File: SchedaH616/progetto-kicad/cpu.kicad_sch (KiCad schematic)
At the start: 81 parts, among them J301 UART0 debug, SW301 RESET, SW302 FEL, U301 H616, U302 TPD4E05U06DQA, U303 TPD4E05U06DQA, U304 TPD4E05U06DQA, U305 TPD4E05U06DQA, U306 TPD4E05U06DQA, U307 TPD4E05U06DQA, U308 TCA6416APWR, Y301 24MHz

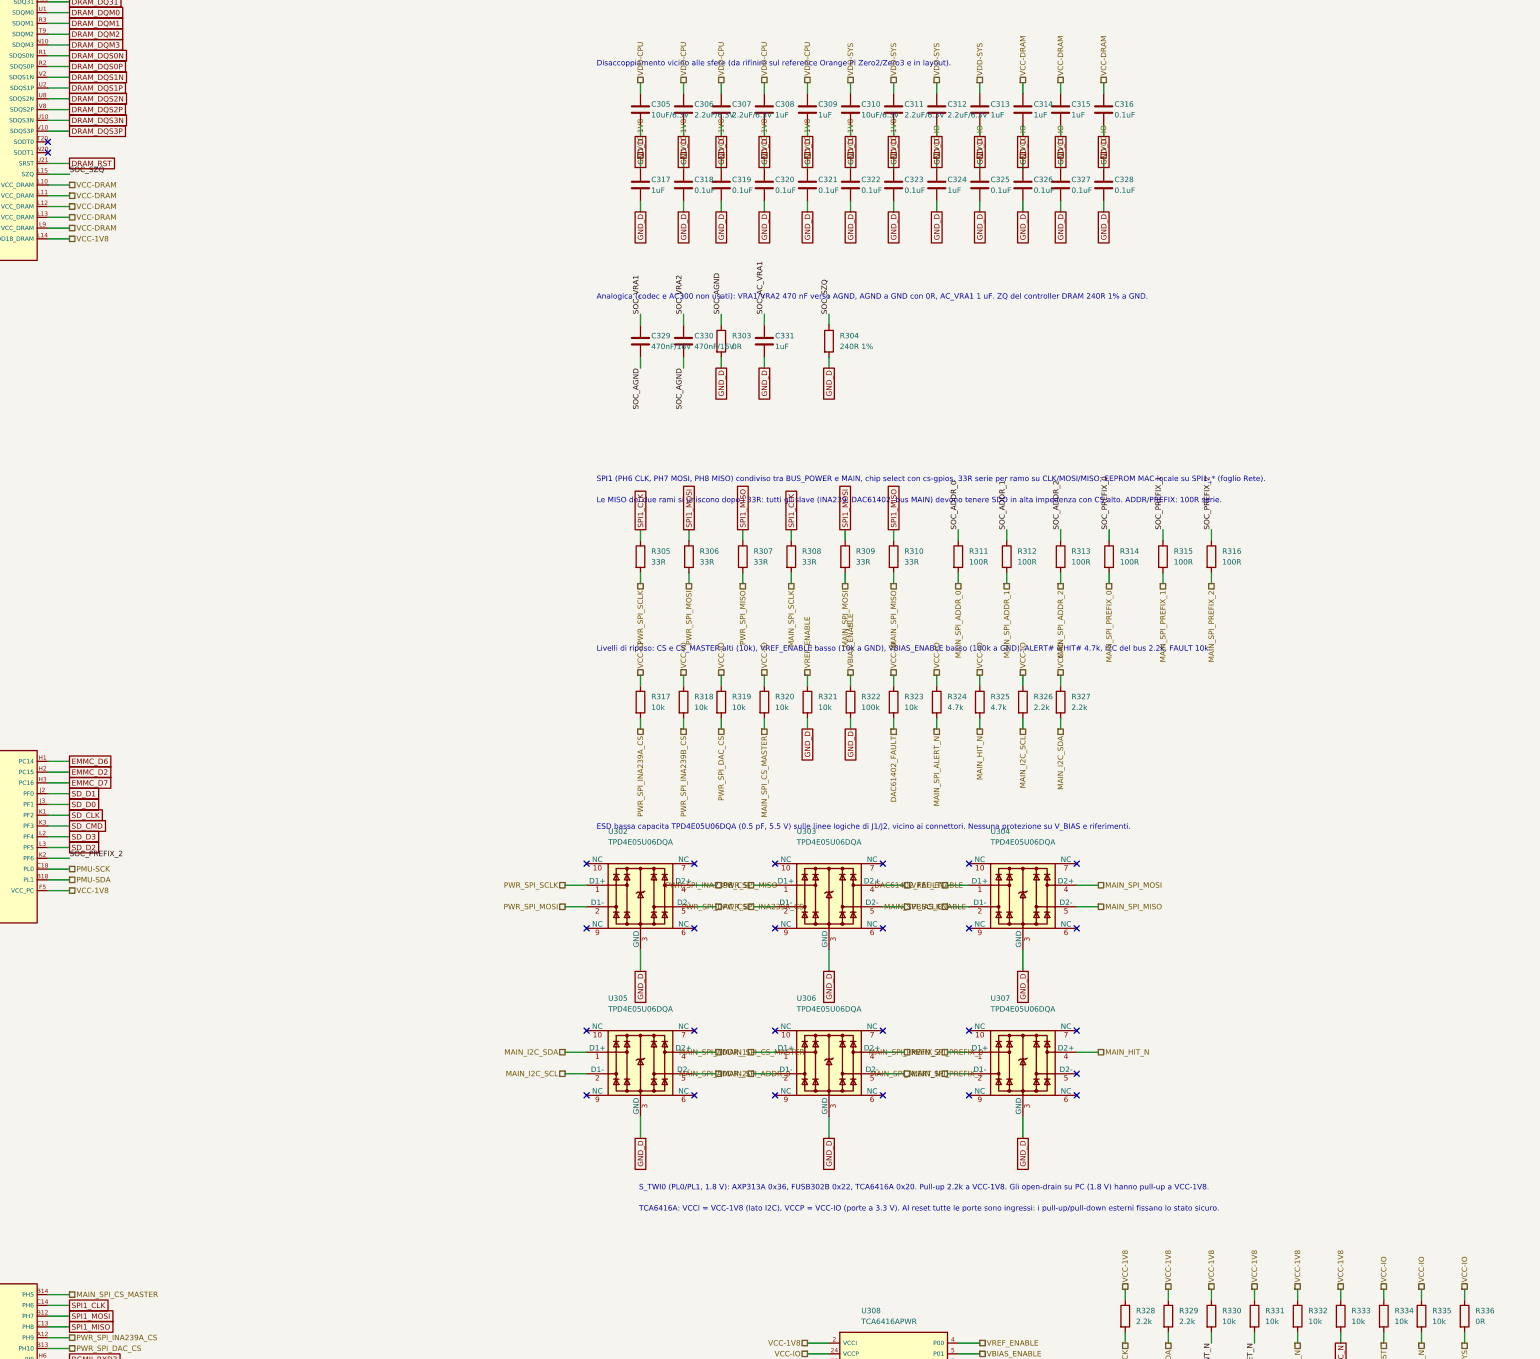
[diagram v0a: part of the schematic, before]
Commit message: SchedaH616: placement PCB 50x70 a 6 strati e modifiche allo schema
PCB (solo placement, niente piste), generato da generatori/build_pcb.sh:
- 50 x 70 mm, smussi 3 mm, 4 fori NPTH 2.2 mm con keepout, 6 strati
- H616 al centro, LPDDR4 sul lato DRAM, AXP313A vicino alla CPU, eMMC vicino ai pin PC
- connettori sui bordi, U.FL Wi-Fi e SMA GNSS su lati opposti
- disaccoppiamento di H616 e LPDDR4 sul bottom sotto le sfere
- regole: piste 5 mil, via-in-pad 0.25/0.15 sotto l'H616
- DRC: 0 violazioni (solo collegamenti da fare), parità schema/PCB ok

Schema (modifiche approvate):
- LPDDR4 confermata come scelta definitiva
- USB host di nuovo su USB-C solo host (Rp 22k, USBLC6-2, TPS2553)
- jack 5 V diretto su IN1 del TPS2121, tolto l'SS54, TPS56637 in Eco-mode
- LDO AP2112K-1.8 (C176944) dedicato a VCCQ eMMC e VCC_PC
- ERC 0

Libreria H616.pretty: serigrafia sui pad tolta, pioli di centraggio NPTH.

Co-Authored-By: Claude Opus 5.5 (1M context) <noreply@anthropic.com>
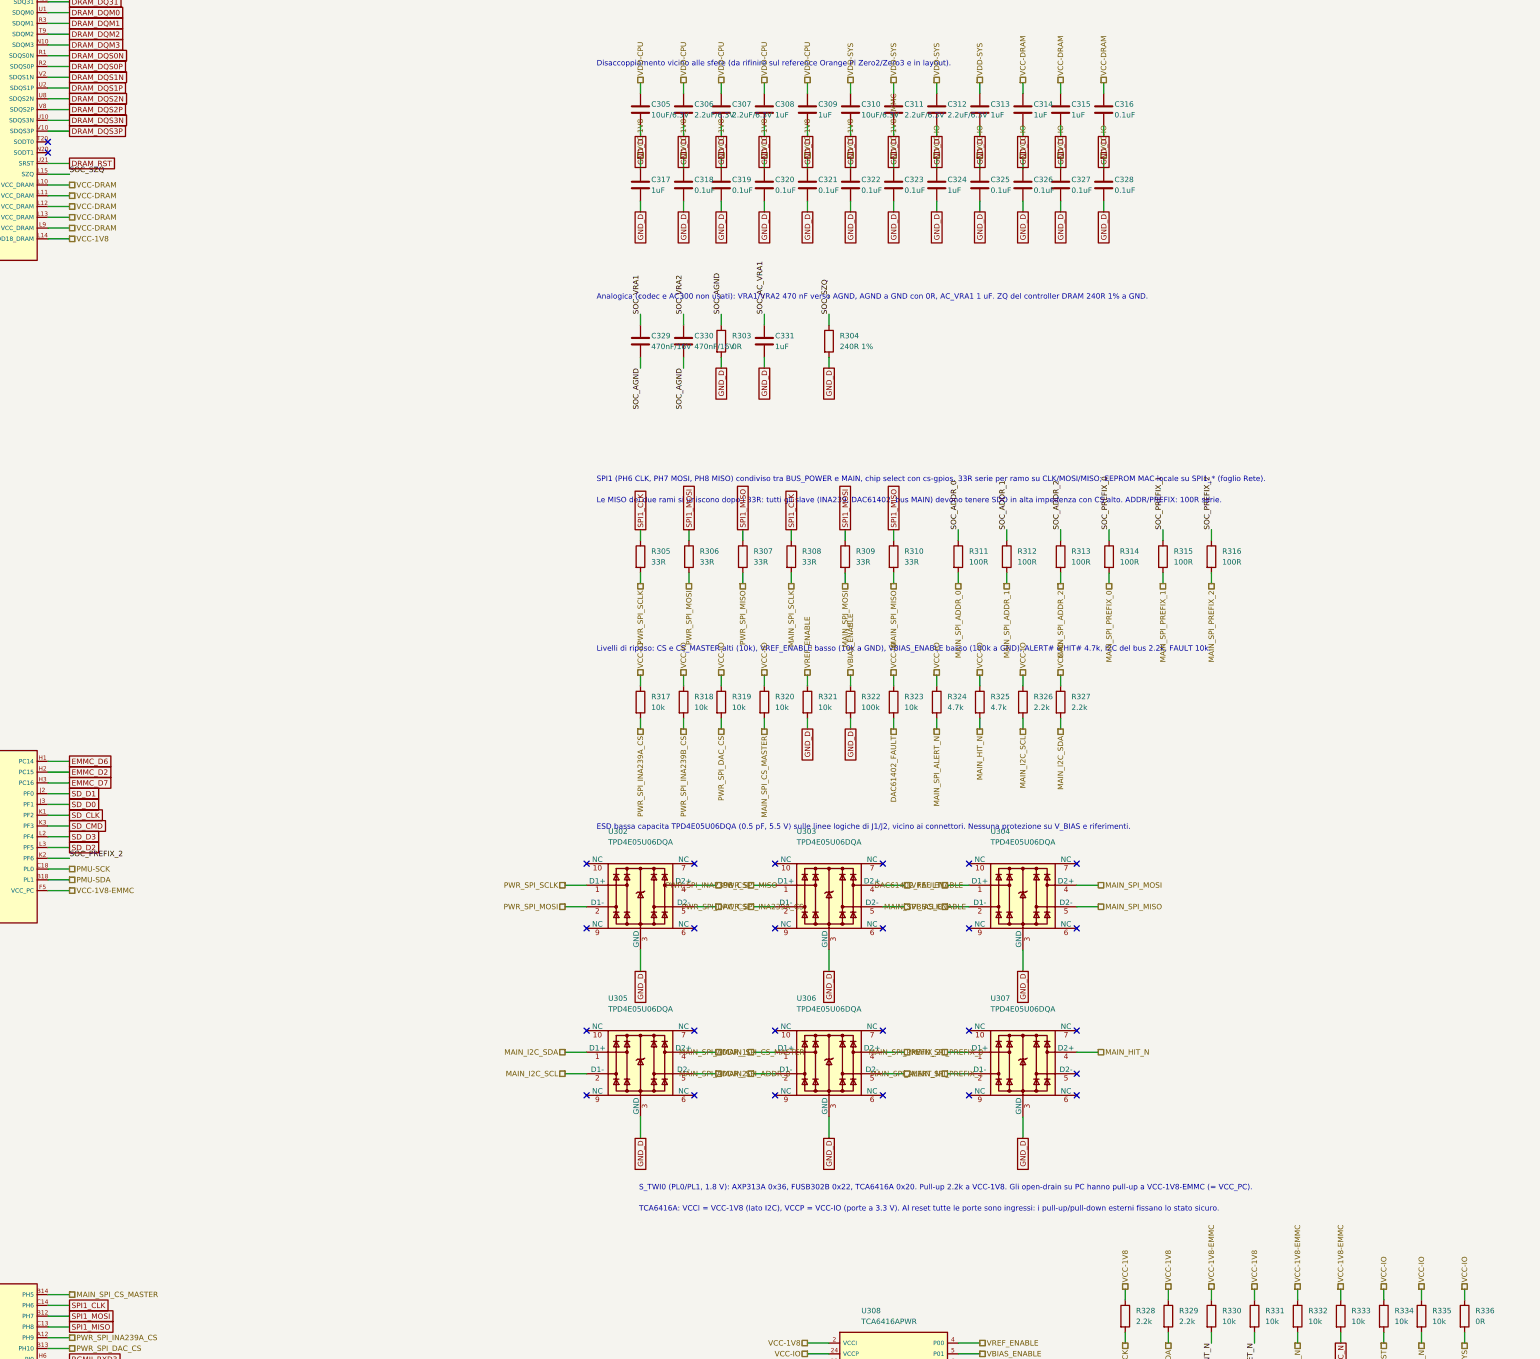
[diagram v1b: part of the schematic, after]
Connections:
- net VCC-1V8: no longer C323.1, R330.1, R332.1, R333.1, U301.F5 (VCC_PC)
- new net VCC-1V8-EMMC: C323.1, R330.1, R332.1, R333.1, U301.F5 (VCC_PC)
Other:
- note added: "S_TWI0 (PL0/PL1, 1.8 V): AXP313A 0x36, FUSB302B 0x22, TCA6416A 0x20. Pull-up 2.2k a VCC-1V8. Gli open-drain su PC hanno pull-up a VCC-1V8-EMMC (= VCC_PC)."
- note removed: "S_TWI0 (PL0/PL1, 1.8 V): AXP313A 0x36, FUSB302B 0x22, TCA6416A 0x20. Pull-up 2.2k a VCC-1V8. Gli open-drain su PC (1.8 V) hanno pull-up a VCC-1V8."

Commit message: SchedaH616: secondo TPS2121 tra buck e jack, controlli dalla Orange Pi Zero2
- TPS2121 U108: IN1 = 5V_BUCK (priorita), IN2 = jack, uscita 5V_EXT verso U103 (IN2 = USB-C)
  PR1 4.49 V, CP2 a GND, OV 5.98 V, ILM 22.1k, ST con test point; priorita bus > jack > USB-C
- TPS56637 di nuovo in FCCM (R114 DNP): il buck ora e' isolato dal jack
- Dalla Orange Pi Zero2 v1.3: REXT 150k 1% ad AGND, AVCC e AC_AVCC 2.2 uF; AC_VRA1 su C17 confermato
- PCB aggiornato: U108 vicino a U103 e al jack
- ERC 0, parita' schema/PCB 0, DRC 0 (solo collegamenti da fare)

Co-Authored-By: Claude Opus 5.5 (1M context) <noreply@anthropic.com>
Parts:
- added C334, C335: 2.2uF/6.3V, Capacitor_SMD:C_0402_1005Metric, symbol Device:C
- added R337: 150k 1%, Resistor_SMD:R_0402_1005Metric, symbol Device:R
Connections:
- net GND_D: now also C334.2, C335.2
- net SOC_AGND: now also R337.2
- net VCC-1V8: now also C334.1, C335.1
- net SOC_REXT: now reaches U301.K18 (REXT)
- net SOC_REXT: now also R337.1
- no-connect marks 74 -> 73
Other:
- note added: "AC_VRA1 su C17 (figura 7-1, footprint EasyEDA e schema Orange Pi Zero2 v1.3; la tabella 4-2 dice D17 per errore). Mappa completa dei pin in docs/pinmap-h616.md."
- note added: "Come Orange Pi Zero2 (H616) v1.3: REXT (K18) 150k 1% ad AGND (R337), AVCC 2.2 uF (C334), AC_AVCC 2.2 uF (C335), AC_VRA1 1 uF su C17."
- note added: "Disaccoppiamento vicino alle sfere. 100 nF su VCC-PLL, VCC_DCXO, VDD18_DRAM, VCC_HDMI, VCC_TV (VCC-1V8) e su VCC_IO, VCC_PG/PI, VCC_USB, VCC_EPHY (VCC-IO), come la Zero2."
- note added: "RESET (dominio VCC_PLL 1.8 V) dal PWROK dell'AXP313A (10k a VCC-1V8 sul foglio PMIC, 1 nF qui) + tasto; FEL a GND con tasto (10k a VCC-IO). JTAG_SEL NC come sulla Zero2 (JTAG su PF). PLLTEST, LRADC liberi."
- note removed: "AC_VRA1: la tabella dice D17, la figura 7-1 e il footprint EasyEDA dicono C17 -> usato C17. Mappa completa dei pin in docs/pinmap-h616.md."
- note removed: "Disaccoppiamento vicino alle sfere (da rifinire sul reference Orange Pi Zero2/Zero3 e in layout)."
- note removed: "RESET (dominio VCC_PLL 1.8 V) dal PWROK dell'AXP313A + tasto; FEL a GND con tasto (pull-up 10k a VCC-IO). JTAG_SEL, PLLTEST, LRADC, REXT liberi."

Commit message: SchedaH616: verifica sullo schema Orange Pi Zero3 (LPDDR4, AXP313A, reset)
- Mappa CA/CS/CK/CKE/RESET della LPDDR4 verificata 8/8 sulla Zero3, sfere della LPDDR4, ODT 100k e ZQ 240R coincidono
- AXP313A allineato alla Zero3: 22 uF sui VIN, 2x47 uF + 1 uF + 100 nF sulle uscite DCDC, DLDO1 47 uF, RTCLDO 4.7 uF, PWRON 100 nF montato
- DCDC3 a 1.1 V impostato dall'SPL di U-Boot (CONFIG_AXP_DCDC3_VOLT)
- RESET H616: 10k a VCC-1V8, 1 nF, 100R in serie da AP-RESET; AC_AVCC 10 uF; quarzo 24 MHz con 12 pF
- scelte-progetto.md: verifiche segnate, differenze volute (VCC_PG 3.3 V, VCC_PC 1.8 V), nuovo punto aperto sugli strap BOOT_SEL
- ERC 0, parita' 0, DRC 0 (solo collegamenti da fare)

Co-Authored-By: Claude Opus 5.5 (1M context) <noreply@anthropic.com>
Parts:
- added R338: 100R, Resistor_SMD:R_0402_1005Metric, symbol Device:R
- added R339: 10k, Resistor_SMD:R_0402_1005Metric, symbol Device:R
- C301, C302: value 18pF/50V -> 12pF/50V
- C335: value 2.2uF/6.3V -> 10uF/6.3V; footprint Capacitor_SMD:C_0402_1005Metric -> Capacitor_SMD:C_0603_1608Metric
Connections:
- net AP-RESET: now also R338.1; no longer C304.1, SW301.1, U301.A16 (RESET)
- net VCC-1V8: now also R339.1
- new net SOC_RESET: C304.1, R338.2, R339.2, SW301.1, U301.A16 (RESET)
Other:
- note added: "Clock: quarzo 24 MHz su DXIN/DXOUT (12 pF come la Zero3, da verificare col carico del quarzo scelto; 0R in serie su DXOUT), DXLDO_OUT 220 nF. L'H616 non ha pin per il quarzo 32 kHz: X32KFOUT (PG10) e' derivato internamente."
- note added: "Come Orange Pi Zero2 (H616) v1.3: REXT (K18) 150k 1% ad AGND (R337), AVCC 2.2 uF (C334), AC_AVCC 10 uF (C335, come la Zero3), AC_VRA1 1 uF su C17."
- note added: "RESET (dominio VCC_PLL 1.8 V): 10k a VCC-1V8 + 1 nF + tasto, 100R in serie dal PWROK dell'AXP313A (AP-RESET), come la Zero3; FEL a GND con tasto (10k a VCC-IO). JTAG_SEL NC come sulla Zero2 (JTAG su PF). PLLTEST, LRADC liberi."
- note removed: "Clock: quarzo 24 MHz su DXIN/DXOUT (18 pF, 0R in serie su DXOUT), DXLDO_OUT 220 nF. L'H616 non ha pin per il quarzo 32 kHz: X32KFOUT (PG10) e' derivato internamente."
- note removed: "Come Orange Pi Zero2 (H616) v1.3: REXT (K18) 150k 1% ad AGND (R337), AVCC 2.2 uF (C334), AC_AVCC 2.2 uF (C335), AC_VRA1 1 uF su C17."
- note removed: "RESET (dominio VCC_PLL 1.8 V) dal PWROK dell'AXP313A (10k a VCC-1V8 sul foglio PMIC, 1 nF qui) + tasto; FEL a GND con tasto (10k a VCC-IO). JTAG_SEL NC come sulla Zero2 (JTAG su PF). PLLTEST, LRADC liberi."

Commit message: SchedaH616: footprint DNP per gli strap BOOT_SEL (PC3-PC6)
- Nessuno strap montato, come la Orange Pi Zero2
- 10k DNP di pull-up (VCC_PC) e pull-down (GND) su PC3, PC4, PC5 (EMMC_CLK), PC6 (EMMC_CMD): R340-R347
- scelte-progetto.md: ordine di boot non verificato, serve lo User Manual H616 §3.4
- ERC 0, parita' 0, DRC 0 (solo collegamenti da fare)

Co-Authored-By: Claude Opus 5.5 (1M context) <noreply@anthropic.com>
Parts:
- added R340, R341, R342, R343, R344, R345, R346, R347: 10k, Resistor_SMD:R_0402_1005Metric, symbol Device:R
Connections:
- net EMMC_CLK: now also R344.2, R345.1
- net EMMC_CMD: now also R346.2, R347.1
- net GND_D: now also R341.2, R343.2, R345.2, R347.2
- net VCC-1V8-EMMC: now also R340.1, R342.1, R344.1, R346.1
- net SOC_BOOT_SEL1: now reaches U301.D1 (PC3)
- net SOC_BOOT_SEL1: now also R340.2, R341.1
- net SOC_BOOT_SEL2: now reaches U301.D2 (PC4)
- net SOC_BOOT_SEL2: now also R342.2, R343.1
- no-connect marks 73 -> 71
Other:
- note added: "Footprint DNP 10k: pull-up a VCC-1V8-EMMC (= VCC_PC) e pull-down a GND su ogni linea. La Zero3 (boot SPI) usa PC3/PC4/PC6 alti e PC5 basso. Su PC5/PC6 (eMMC) metterli sui via, senza stub."
- note added: "Strap BOOT_SEL[4:1] = PC6/PC5/PC4/PC3: nessuno montato, come la Zero2 (la tabella livelli -> supporto e' nello User Manual H616 par. 3.4, non disponibile)."

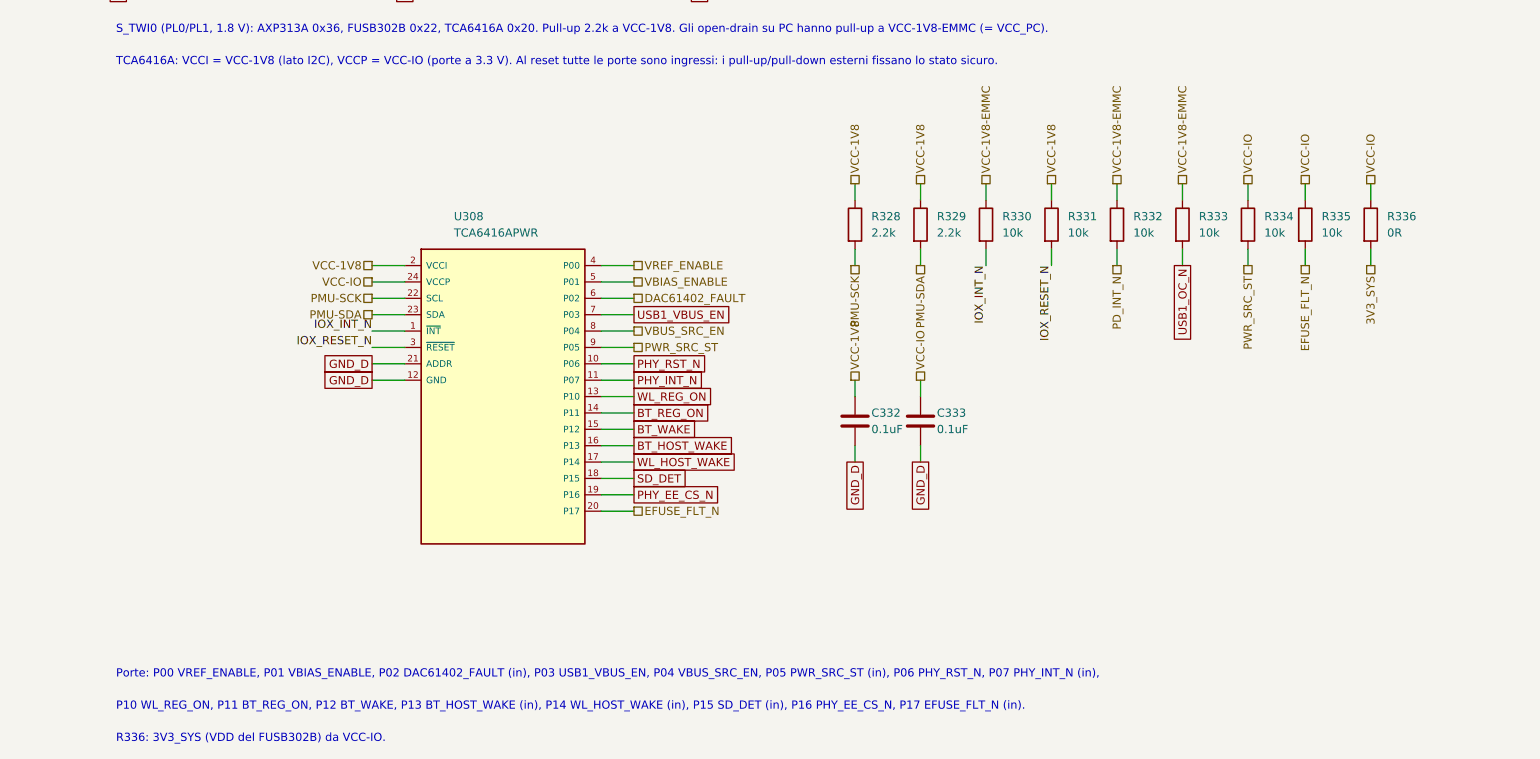
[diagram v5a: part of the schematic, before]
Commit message: SchedaH616: eFuse TPS259470 eliminato
- tolti U106 TPS259470 e i suoi componenti (partitore UVLO/OVLO, RILM, dVdT, 1 uF d'ingresso) e il footprint RPW dalla libreria
- VIN_SYS dal BUS_POWER direttamente all'ingresso del TPS56637 (restano C101/C102 10 uF e C125 100 nF)
- ingresso 12 V senza limite di corrente, OVP ne' blocco inverso; nessuna TVS sui 12 V
- P17 del TCA6416A ora libera; documenti aggiornati
- ERC 0, parita' 0, DRC 0 (solo collegamenti da fare)

Co-Authored-By: Claude Opus 5.5 (1M context) <noreply@anthropic.com>
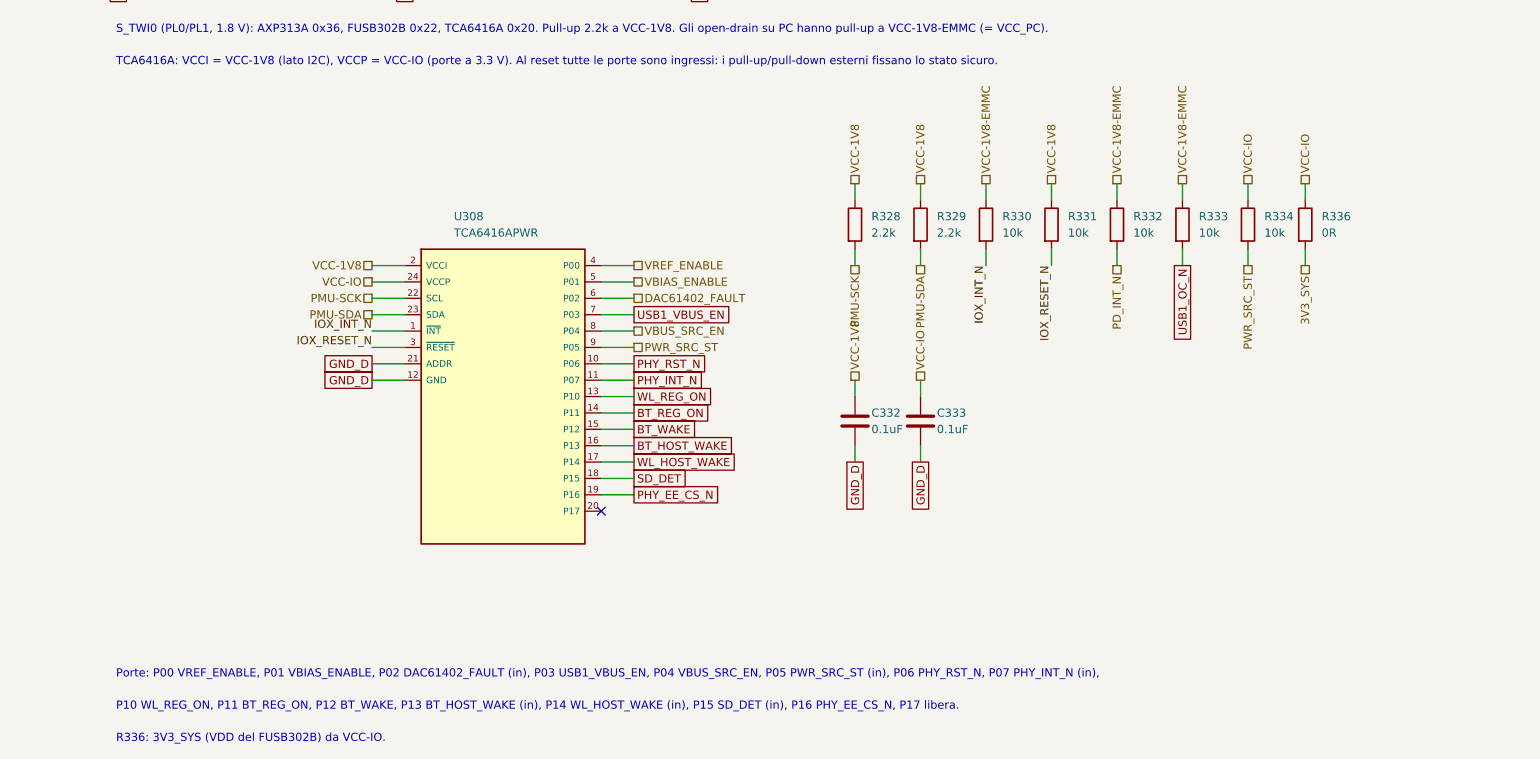
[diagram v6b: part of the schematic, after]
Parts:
- removed R335: 10k, Resistor_SMD:R_0402_1005Metric, symbol Device:R
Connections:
- net EFUSE_FLT_N: no longer names the net of U308.20 (P17)
- no-connect marks 71 -> 72
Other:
- note added: "P10 WL_REG_ON, P11 BT_REG_ON, P12 BT_WAKE, P13 BT_HOST_WAKE (in), P14 WL_HOST_WAKE (in), P15 SD_DET (in), P16 PHY_EE_CS_N, P17 libera."
- note removed: "P10 WL_REG_ON, P11 BT_REG_ON, P12 BT_WAKE, P13 BT_HOST_WAKE (in), P14 WL_HOST_WAKE (in), P15 SD_DET (in), P16 PHY_EE_CS_N, P17 EFUSE_FLT_N (in)."
